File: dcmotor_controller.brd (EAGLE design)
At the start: 160 x 100 mm, 81 parts, among them IC1 L298, IC2 L298, IC5 SN74LVCR162245A, Q1 MOSFET-PCHANNEL_SOT23-3, Q2 8MHz, T1 BC857BS, T14 BSS306N, U2 STM32F10XRXT6

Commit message: update - clean - parts
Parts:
- C25, C26, C27, C28, C29, C30, C31, C32: device rcl:C025-024X044 -> rcl:C0805
- D17: value SMBJ5.0A-TR -> SMBJ5.0A
- R10, R11, R12, R13, R14: device rcl:0204/5 -> rcl:R0805
- moved R12 1.80 mm to (86.4, 8.89), flipped to the bottom
- moved R13 1.27 mm to (80.0, 63.5)
- flipped C10 to the top
- renumbered POWER_CON to PWR
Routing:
- net 5V: track 192.4 -> 198.8 mm
- net 3V3: track 327.3 -> 321.0 mm, vias 14 -> 15
- net BOOTO: track 37.4 -> 34.0 mm, vias 1 -> 2
- net GND: track 914.9 -> 917.6 mm, vias 7 -> 5
- net SPI1_NSS: track 96.0 -> 97.6 mm
- net SDA: track 44.0 -> 45.6 mm
- net OSC_IN: track 25.4 -> 24.3 mm, vias 1 -> 0
- net SCL: track 48.8 -> 49.6 mm
- net OSC_OUT: track 40.8 -> 40.1 mm, vias 1 -> 0

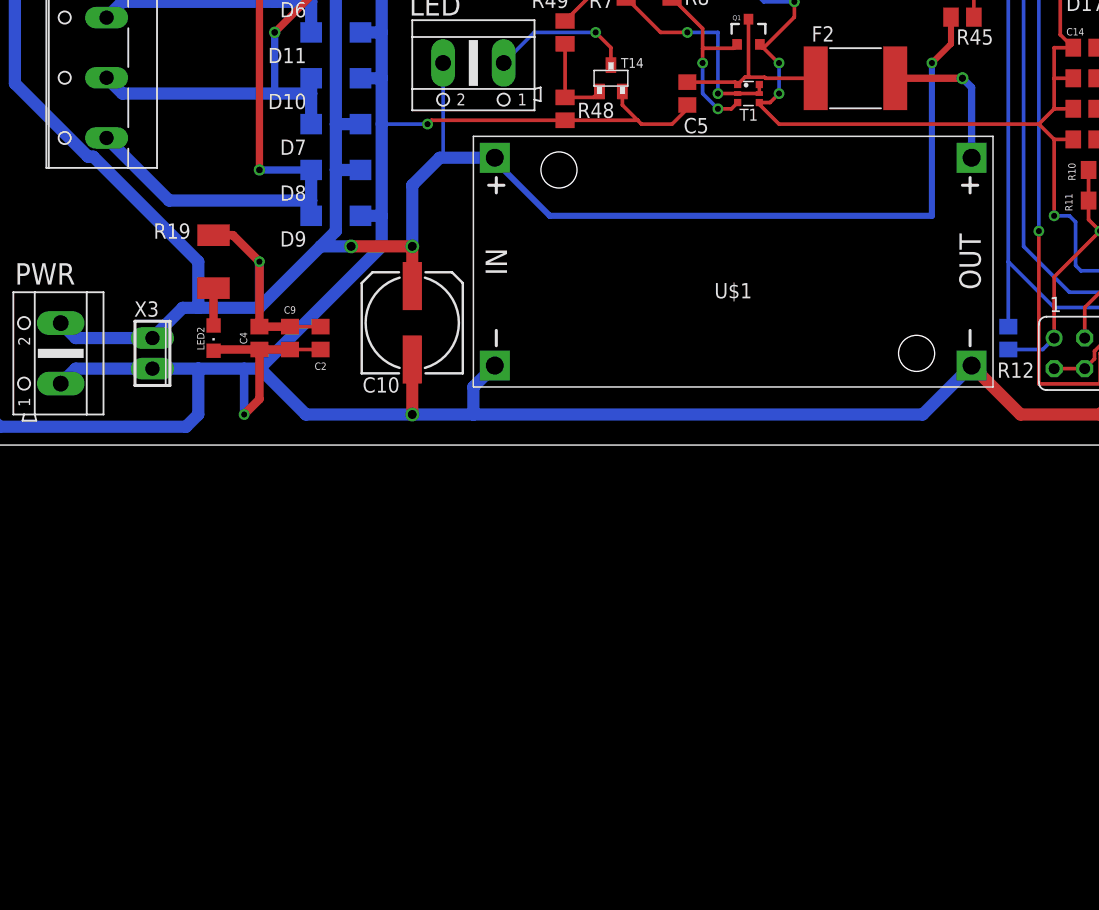
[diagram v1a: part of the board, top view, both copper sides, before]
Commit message: 3dmodel added
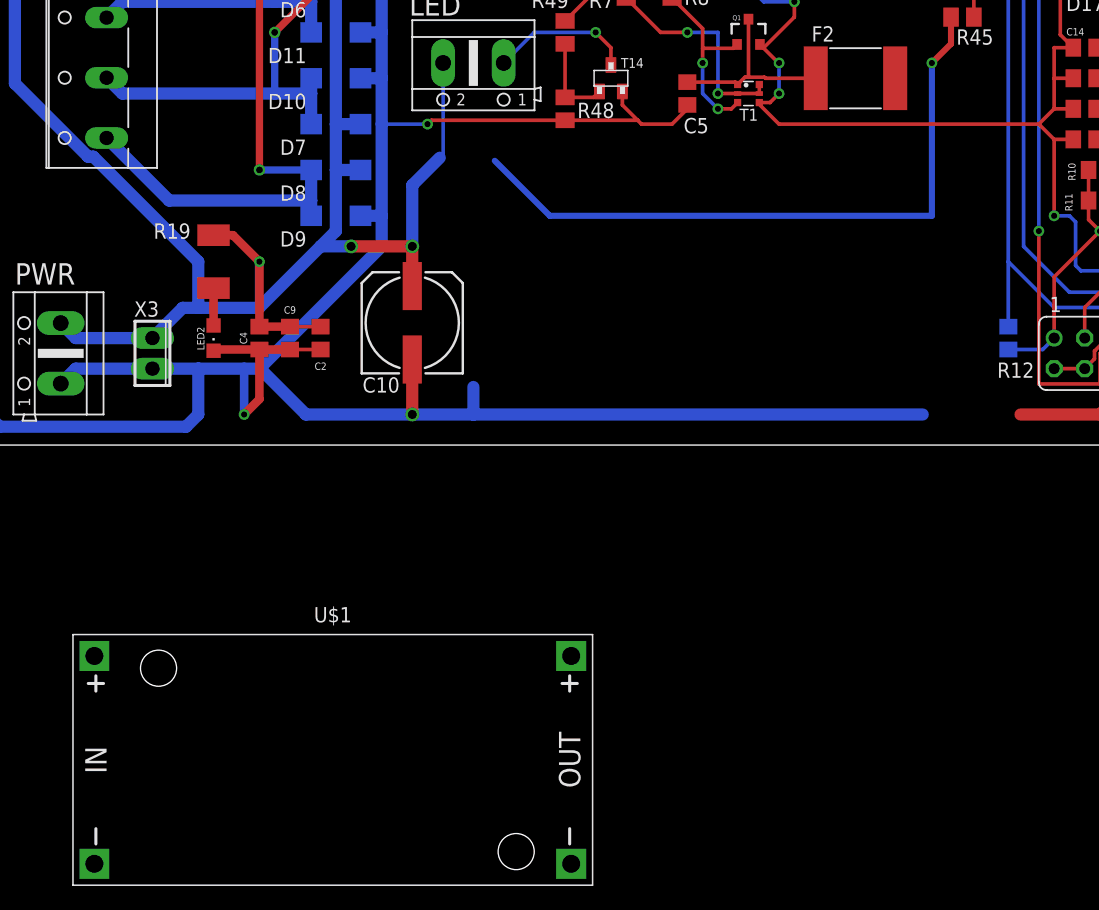
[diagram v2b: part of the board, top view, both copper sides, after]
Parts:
- moved U$1 53.1 mm to (30.2, -26.2)
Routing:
- net GND: track 917.6 -> 903.6 mm
- net N$1: track 12.5 -> 0.00 mm, vias 1 -> 0
- net 24V: track 354.5 -> 349.6 mm
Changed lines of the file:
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@@
 <drawing>
 <settings>
-<setting alwaysvectorfont="no"/>
+<setting alwaysvectorfont="yes"/>
 <setting verticaltext="up"/>
 </settings>
@@
 </layers>
 <board>
+<fusionsync huburn="a.cGVyc29uYWw6dWUyODdlZWVl" projecturn="a.cGVyc29uYWw6dWUyODdlZWVlIzIwMTgwNDA4MTI2NTg3MzI2" f3durn="urn:adsk.wipprod:dm.lineage:cQiRumaYQySxqMgdQmJA_w" pcbguid="6678936a-43be-4169-baa4-ea48a086b149" lastpulledtime="" lastsyncedchangeguid="47db0d4f-7243-e3a9-a740-30e95a28c65b"/>
 <plain>
 <wire x1="0" y1="0" x2="160" y2="0" width="0" layer="20"/>
@@
 <attribute name="NAME" x="55.118" y="31.75" size="0.8128" layer="25" font="vector" ratio="10" align="center"/>
 </element>
-<element name="U$1" library="lm2596" library_urn="urn:adsk.eagle:library:2557020" package="DC-DC-STEP-DOWN-LM2596" package3d_urn="urn:adsk.eagle:package:2557271/1" value="DC-DC-STEP-DOWN-LM2596" x="63.5" y="15.24" smashed="yes">
-<attribute name="NAME" x="63.5" y="12.192" size="1.27" layer="25" align="bottom-center"/>
-<attribute name="VALUE" x="63.5" y="6.604" size="1.27" layer="27" align="top-center"/>
-</element>
 <element name="U2" library="stm32" package="TQFP64" value="STM32F10XRXT6" x="93.98" y="54.61" smashed="yes">
 <attribute name="NAME" x="98.044" y="59.436" size="1.778" layer="25"/>
@@
 <attribute name="VALUE" x="12.192" y="10.414" size="1.27" layer="27" rot="R270"/>
 </element>
+<element name="U$1" library="lm2596" library_urn="urn:adsk.eagle:library:2557020" package="DC-DC-STEP-DOWN-LM2596" package3d_urn="urn:adsk.eagle:package:2557271/2" value="DC-DC-STEP-DOWN-LM2596" x="30.226" y="-26.162"/>
 </elements>
 <signals>
@@
 <contactref element="C3" pad="1"/>
 <contactref element="C4" pad="2"/>
-<contactref element="U$1" pad="IN-"/>
-<contactref element="U$1" pad="OUT-"/>
 <contactref element="C5" pad="2"/>
 <contactref element="R8" pad="1"/>
@@
 <wire x1="34.29" y1="63.5" x2="34.29" y2="55.88" width="1.016" layer="16"/>
 <wire x1="34.29" y1="55.88" x2="32.53" y2="55.88" width="1.016" layer="16"/>
-<wire x1="83.312" y1="6.604" x2="79.248" y2="2.54" width="1.016" layer="16"/>
 <wire x1="79.248" y1="2.54" x2="41.91" y2="2.54" width="1.016" layer="16"/>
 <wire x1="41.91" y1="2.54" x2="41.91" y2="4.826" width="1.016" layer="16"/>
-<wire x1="41.91" y1="4.826" x2="43.688" y2="6.604" width="1.016" layer="16"/>
 <wire x1="95.25" y1="3.81" x2="93.98" y2="2.54" width="1.016" layer="1"/>
 <wire x1="95.25" y1="3.81" x2="95.25" y2="6.35" width="1.016" layer="1"/>
@@
 <via x="36.83" y="2.54" extent="1-16" drill="0.75"/>
 <wire x1="93.98" y1="2.54" x2="87.376" y2="2.54" width="1.016" layer="1"/>
-<wire x1="87.376" y1="2.54" x2="83.312" y2="6.604" width="1.016" layer="1"/>
+<contactref element="U$1" pad="IN-"/>
+<contactref element="U$1" pad="OUT-"/>
+<wire x1="79.248" y1="2.54" x2="87.376" y2="2.54" width="0" layer="19" extent="1-16"/>
+<wire x1="10.414" y1="-34.798" x2="18.034" y2="1.524" width="0" layer="19" extent="16-16"/>
+<wire x1="50.038" y1="-34.798" x2="41.91" y2="2.54" width="0" layer="19" extent="16-16"/>
 </signal>
 <signal name="SEN4">
@@
 <contactref element="X3" pad="1"/>
 <contactref element="R19" pad="1"/>
-<contactref element="U$1" pad="IN+"/>
 <wire x1="30.48" y1="74.93" x2="30.48" y2="67.31" width="1.016" layer="16"/>
 <wire x1="30.48" y1="67.31" x2="30.48" y2="59.69" width="1.016" layer="16"/>
@@
 <via x="31.75" y="16.51" extent="1-16" drill="0.75"/>
 <wire x1="31.75" y1="16.51" x2="29.21" y2="16.51" width="1.016" layer="16"/>
-<wire x1="43.688" y1="23.876" x2="39.116" y2="23.876" width="1.016" layer="16"/>
 <wire x1="36.83" y1="21.59" x2="36.83" y2="16.51" width="1.016" layer="16"/>
 <wire x1="39.116" y1="23.876" x2="36.83" y2="21.59" width="1.016" layer="16"/>
@@
 <wire x1="24.13" y1="9.84" x2="26.67" y2="9.84" width="0.7112" layer="1"/>
 <wire x1="29.21" y1="9.84" x2="26.67" y2="9.84" width="0.3048" layer="1"/>
-<wire x1="43.688" y1="23.876" x2="43.688" y2="23.622" width="0.508" layer="16"/>
 <wire x1="48.26" y1="19.05" x2="80.01" y2="19.05" width="0.508" layer="16"/>
 <wire x1="80.01" y1="19.05" x2="80.01" y2="31.75" width="0.508" layer="16"/>
@@
 <wire x1="81.6" y1="33.34" x2="81.6" y2="35.56" width="0.508" layer="1"/>
 <wire x1="43.688" y1="23.622" x2="48.26" y2="19.05" width="0.508" layer="16"/>
+<contactref element="U$1" pad="IN+"/>
+<wire x1="39.3954" y1="24.1554" x2="43.688" y2="23.622" width="0" layer="19" extent="16-16"/>
+<wire x1="10.414" y1="-17.526" x2="8.8646" y2="8.89" width="0" layer="19" extent="16-16"/>
 </signal>
 <signal name="5V">
@@
 <wire x1="90.17" y1="19.05" x2="90.17" y2="25.4" width="0.3048" layer="1"/>
 </signal>
-<signal name="N$5">
-<contactref element="U$1" pad="OUT+"/>
-<contactref element="F2" pad="2"/>
-<wire x1="83.312" y1="23.876" x2="83.312" y2="29.718" width="0.6096" layer="16"/>
-<wire x1="83.312" y1="29.718" x2="82.55" y2="30.48" width="0.6096" layer="16"/>
-<via x="82.55" y="30.48" extent="1-16" drill="0.6"/>
-<wire x1="76.96" y1="30.48" x2="82.55" y2="30.48" width="0.6096" layer="1"/>
-</signal>
 <signal name="N$6">
 <contactref element="F2" pad="1"/>
@@
 <wire x1="63.87" y1="29.21" x2="65.67" y2="29.21" width="0.3048" layer="1"/>
 </signal>
+<signal name="N$1">
+<contactref element="U$1" pad="OUT+"/>
+<contactref element="F2" pad="2"/>
+<wire x1="50.038" y1="-17.526" x2="76.96" y2="30.48" width="0" layer="19" extent="1-1"/>
+</signal>
 </signals>
 </board>
@@
 </note>
 <note version="8.3" severity="warning">
+Since Version 8.3, EAGLE supports Fusion synchronisation.
+This feature will not be available in this version and saving
+the document will break the link to the Fusion PCB feature.
+</note>
+<note version="8.3" severity="warning">

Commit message: Add files via upload
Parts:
- moved U$1 52.1 mm to (62.2, 15.0)
- moved SV2 34.1 mm to (119.9, 75.9), turned to 0 degrees
- moved C21 28.7 mm to (80.3, 84.8)
- moved R20 28.6 mm to (83.8, 85.3)
- moved C11 26.9 mm to (87.4, 84.8)
- moved R3 26.9 mm to (90.9, 85.3)
- moved R4 25.4 mm to (98.3, 85.3)
- moved C12 25.4 mm to (94.7, 85.3)
- moved SV5 25.0 mm to (128.5, 21.3)
- moved SV4 24.2 mm to (128.5, 41.9)
- moved R5 24.2 mm to (105.9, 85.3)
- moved C13 24.1 mm to (102.4, 85.3)
- moved SV3 23.9 mm to (128.5, 62.5)
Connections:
- removed net MISO: U2.56
- removed net MOSI: U2.57
- removed net SCK: U2.55
- net CLK: now also U2.61
- net CSN: now also U2.62
- net RPI_CLK: now also U2.55
- net RPI_MISO: now also U2.56
- net RPI_MOSI: now also U2.57
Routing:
- net RPI_MISO: track 0.00 -> 89.8 mm, vias 0 -> 6
- net RPI_MOSI: track 0.00 -> 89.2 mm, vias 0 -> 4
- net RPI_CLK: track 0.00 -> 88.2 mm, vias 0 -> 7
- net CSN: track 82.9 -> 140.0 mm, vias 4 -> 10
- net CLK: track 85.4 -> 141.3 mm, vias 0 -> 7
- net 3V3: track 321.0 -> 274.6 mm, vias 15 -> 8
- net A_LSB_U1: track 84.0 -> 38.5 mm, vias 2 -> 3
- net B_DIR_V4: track 107.1 -> 72.6 mm, vias 2 -> 3
- net B_DIR_V1: track 73.7 -> 40.4 mm, vias 2 -> 1
- net INDEX_W1: track 77.5 -> 44.4 mm, vias 2 -> 3
- net GND: track 903.6 -> 874.0 mm, vias 5 -> 7
- net SEN1: track 120.8 -> 93.4 mm
- net A_LSB_U3: track 60.6 -> 34.3 mm, vias 2 -> 1
- net INDEX_W3: track 62.8 -> 36.8 mm, vias 2 -> 3
- net SEN2: track 89.3 -> 112.5 mm
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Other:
- board size 160 x 100 mm -> 142.2 x 90.6 mm
- board text added: "SCORPIO JUNIOR BOARD"

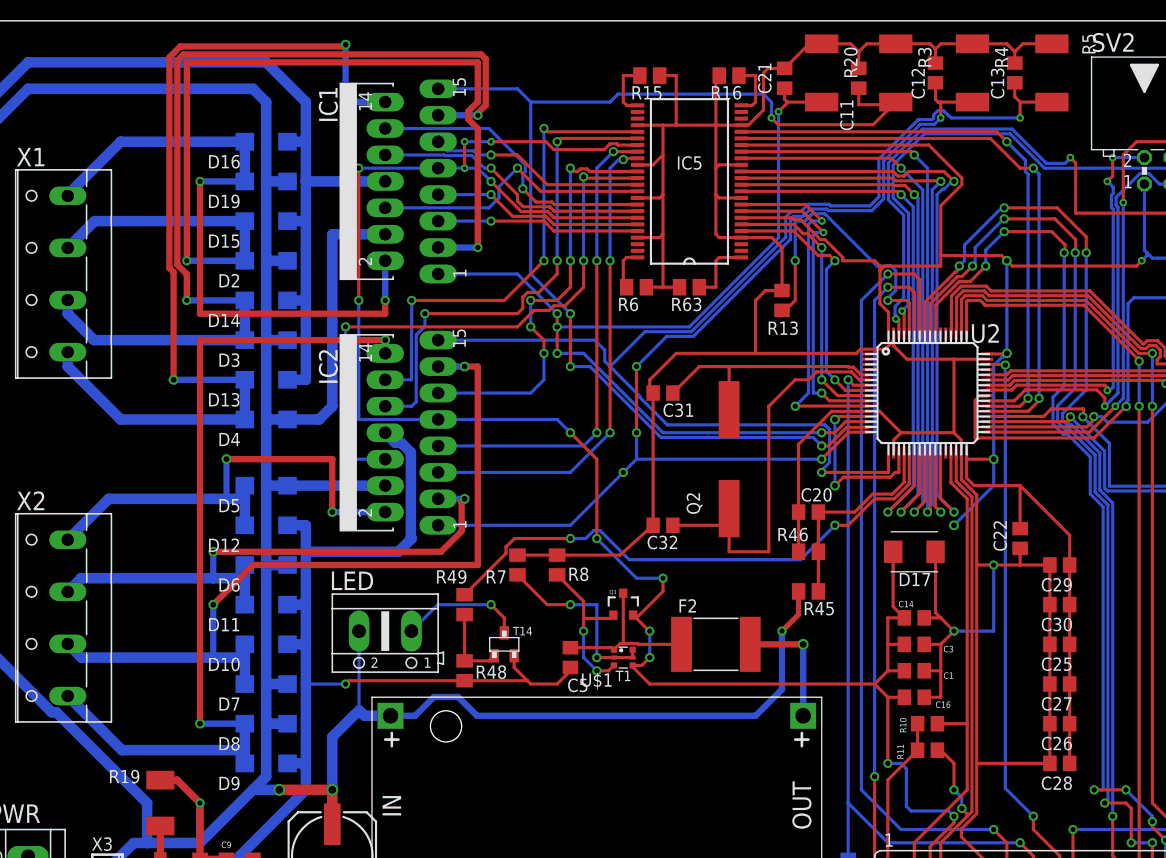
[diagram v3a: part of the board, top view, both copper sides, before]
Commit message: airwires connected, names
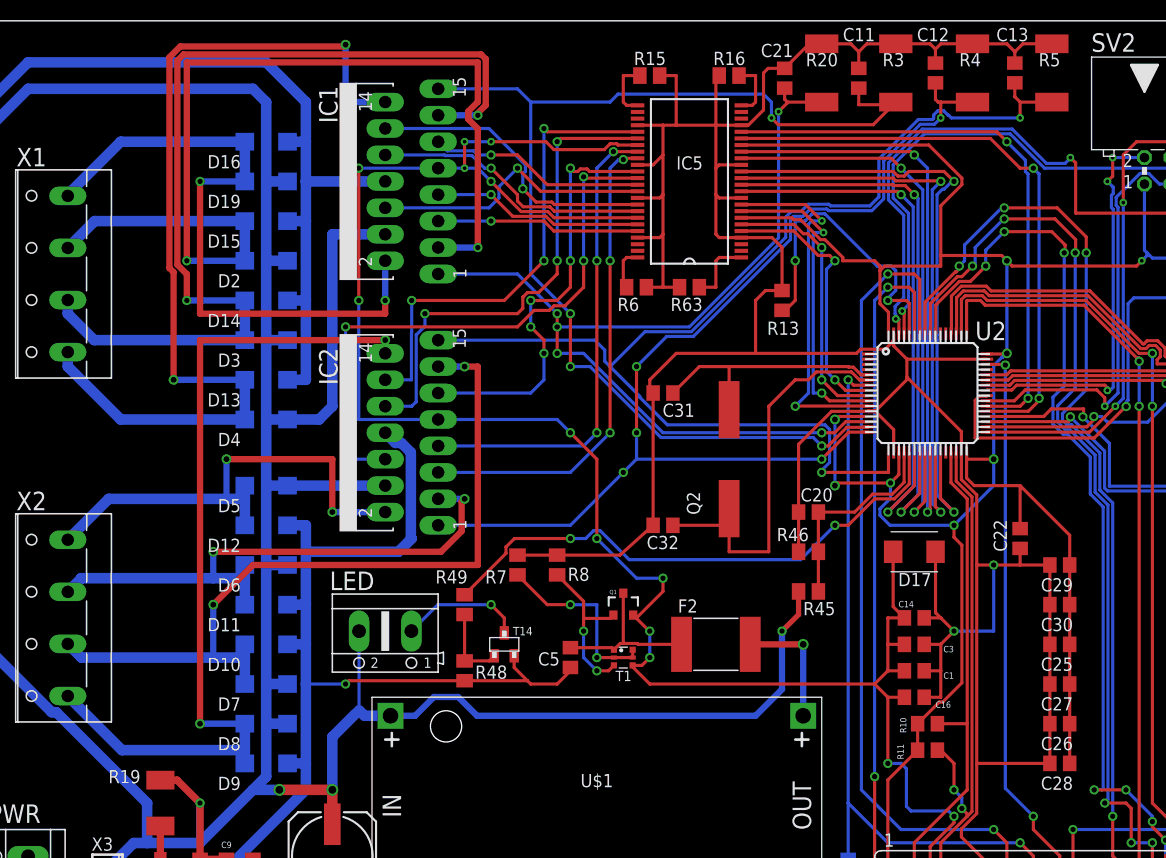
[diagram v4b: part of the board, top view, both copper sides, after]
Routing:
- net 3V3: track 274.6 -> 307.1 mm, vias 8 -> 9
- net GND: track 874.0 -> 875.1 mm
